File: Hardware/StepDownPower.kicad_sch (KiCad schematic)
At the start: 9 parts, among them J7 VXO7805-500-M-TR, J8 3557-2

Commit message: Added changes to logic side for comparator inputs
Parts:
- added C12: 47uF, Capacitor_SMD:C_0603_1608Metric, symbol Device:C_Small
- added C13: 22uF, Capacitor_SMD:C_0603_1608Metric, symbol Device:C_Small
- added IC1: TR05S3V3, Converter_DCDC:TR05S3V3, symbol Converter_DCDC:TR05S3V3
- C5: footprint (none) -> Capacitor_SMD:C_0603_1608Metric
- L1, L2: footprint (none) -> Inductor_SMD:L_Sumida_CDMC6D28_7.25x6.5mm
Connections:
- net +12V: now also C13.1, IC1.1 (+VIN)
- net GND: now also C12.2, C13.2, IC1.2 (GND)
- new net +3.3V: C12.1, IC1.3 (+VOUT)
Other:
- note added: "12 to 3.3v"
- note added: "12 to 5V"

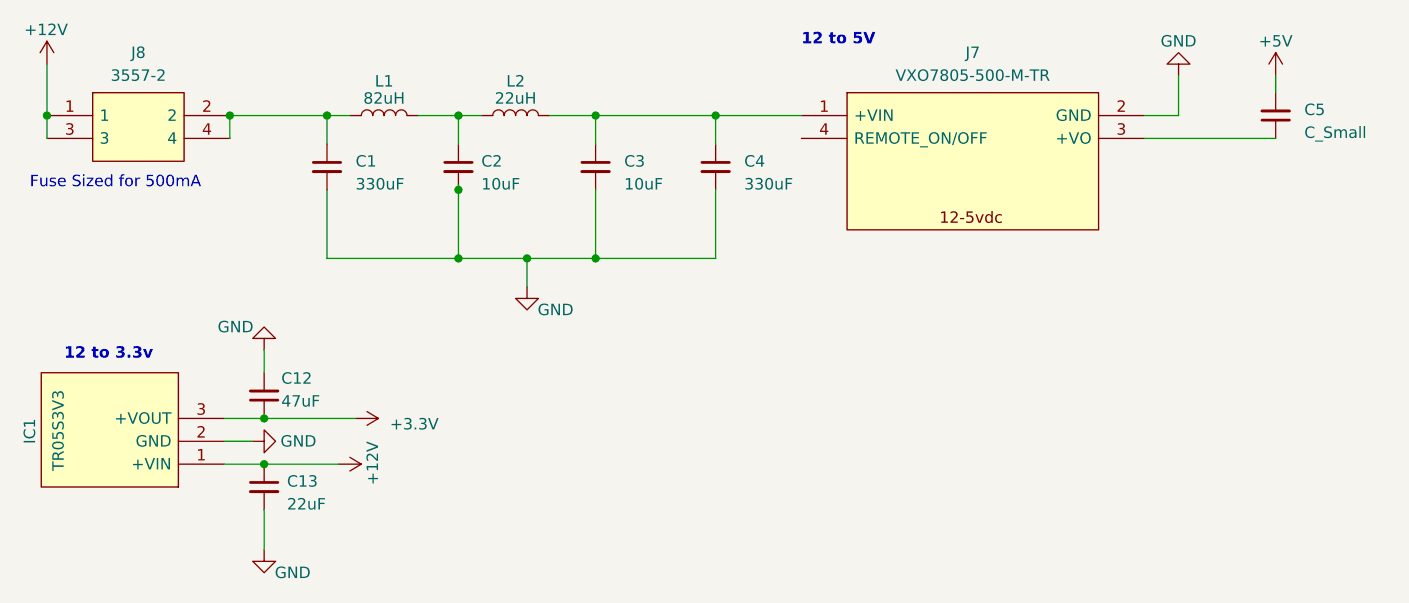
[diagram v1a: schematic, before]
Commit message: Removed a lot of unnecessary BJT logic, removed rotary switches for logic setting (set all to universal final 3.3v based logic)
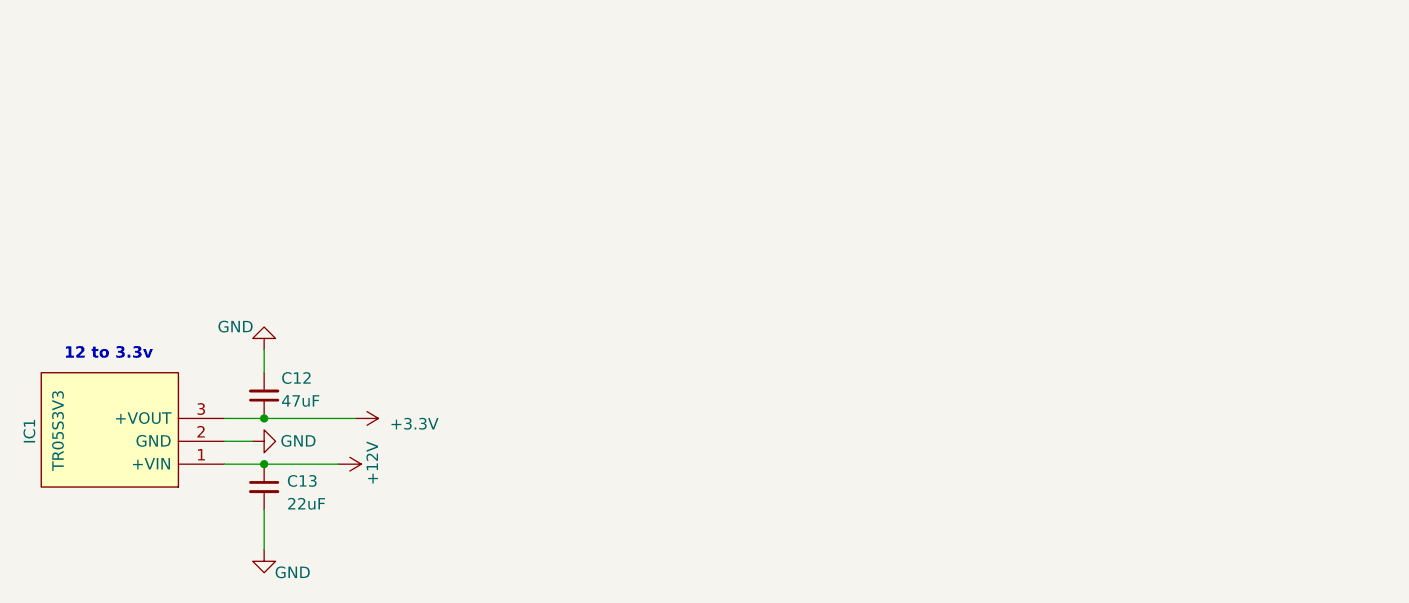
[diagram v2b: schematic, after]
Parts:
- removed C1, C4: 330uF, Capacitor_SMD:C_0603_1608Metric, symbol Device:C_Small
- removed C2, C3: 10uF, Capacitor_SMD:C_0603_1608Metric, symbol Device:C_Small
- removed C5: C_Small, Capacitor_SMD:C_0603_1608Metric, symbol Device:C_Small
- removed J7: VXO7805-500-M-TR, Converter_DCDC:VXO7805500MTR, symbol Regulator_Switching:VXO7805-500-M-TR
- removed J8: 3557-2, Fuse:3557-2, symbol Device:3557-2
- removed L1: 82uH, Inductor_SMD:L_Sumida_CDMC6D28_7.25x6.5mm, symbol Device:L
- removed L2: 22uH, Inductor_SMD:L_Sumida_CDMC6D28_7.25x6.5mm, symbol Device:L
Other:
- note removed: "12 to 5V"
- note removed: "Fuse Sized for 500mA"
